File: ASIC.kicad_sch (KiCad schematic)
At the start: 76 parts, among them U1 MCP1824T-1202E/OT, U3 MCP1824T-1202E/OT, U4 MCP1824T-1202E/OT, U6 MCP1824T-1202E/OT, U8 SN74AXC4T774, Y2 50MHz

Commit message: move over to bitaxeBlock ASIC sheet
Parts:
- removed A1, A3: BZM2_MODE0, bitaxe:bzm2, symbol bitaxe:BZM2_mode0
- removed A2, A4: BZM2_MODE1, bitaxe:bzm2, symbol bitaxe:BZM2_mode1
- removed C19, C26, C27, C28, C7: 1uF, Capacitor_SMD:C_0402_1005Metric, symbol Device:C_Small
- removed C58: 0.1uF, Capacitor_SMD:C_0402_1005Metric, symbol Device:C_Small
- removed C60, C62, C63, C64: 120pF, Capacitor_SMD:C_0402_1005Metric, symbol Device:C_Small
- removed R4: 1k, Resistor_SMD:R_0402_1005Metric, symbol Device:R_Small_US
- removed R9: 10k, Resistor_SMD:R_0402_1005Metric, symbol Device:R_Small_US
- removed TP13, TP32, TP51, TP55: RSTI, bitaxe:TestPoint_Pad_1.0x0.4mm, symbol Connector:TestPoint
- removed TP14, TP31, TP38, TP46: RXO, bitaxe:TestPoint_Pad_1.0x0.4mm, symbol Connector:TestPoint
- removed TP17, TP33, TP40, TP50, TP54: TXO, bitaxe:TestPoint_Pad_1.0x0.4mm, symbol Connector:TestPoint
- removed TP18: 1V2-1, bitaxe:TestPoint_Pad_D1.0mm, symbol Connector:TestPoint
- removed TP20, TP36, TP52, TP56: RXI, bitaxe:TestPoint_Pad_1.0x0.4mm, symbol Connector:TestPoint
- removed TP21, TP34, TP41, TP49, TP53: TTO, bitaxe:TestPoint_Pad_1.0x0.4mm, symbol Connector:TestPoint
- removed TP22: GND, bitaxe:TestPoint_Pad_1.0x0.4mm, symbol Connector:TestPoint
- removed TP28, TP43: TTI, bitaxe:TestPoint_Pad_1.0x0.4mm, symbol Connector:TestPoint
- removed TP29, TP44: TXI, bitaxe:TestPoint_Pad_1.0x0.4mm, symbol Connector:TestPoint
- removed TP3: 1V2-3, bitaxe:TestPoint_Pad_D1.0mm, symbol Connector:TestPoint
- removed TP30, TP39, TP45: RSTO, bitaxe:TestPoint_Pad_1.0x0.4mm, symbol Connector:TestPoint
- removed TP35, TP48, TP57: CLKI, bitaxe:TestPoint_Pad_1.0x0.4mm, symbol Connector:TestPoint
- removed TP37, TP42, TP47: CLKO, bitaxe:TestPoint_Pad_1.0x0.4mm, symbol Connector:TestPoint
- removed TP58: D1, bitaxe:TestPoint_Pad_D1.0mm, symbol Connector:TestPoint
- removed TP59: D2, bitaxe:TestPoint_Pad_D1.0mm, symbol Connector:TestPoint
- removed TP60: D3, bitaxe:TestPoint_Pad_D1.0mm, symbol Connector:TestPoint
- removed U1, U3, U4, U6: MCP1824T-1202E/OT, bitaxe:SOT-23-5, symbol bitaxe:MCP1824
- removed U8: SN74AXC4T774, bitaxe:BQB0016A-MFG, symbol bitaxe:SN74AVC4T774-BQB
- removed Y2: 50MHz, bitaxe:OSC_ECS-3225MV-500-CN-TR, symbol bitaxe:oscillator
- added A1, A2: ProtoMC3, bitaxe:proto-mc3, symbol bitaxe:BlockMC3_mode0
- added A3, A4: ProtoMC3, bitaxe:proto-mc3, symbol bitaxe:BlockMC3_mode1
- added C100, C101, C102, C103, C104, C105, C106, C107, C108, C109, C110, C111, C112, C113, C114, C115, C116, C117, C118, C119, C120, C121, C122, C123, C124, C125, C126, C127, C128, C129, C209, C49, C50, C53, C54, C55, C56, C98, C99: 1uF, Capacitor_SMD:C_0402_1005Metric, symbol Device:C_Small
- added C130, C208, C51, C52, C84, C86, C88, C90, C91, C96: 0.1uF, Capacitor_SMD:C_0402_1005Metric, symbol Device:C_Small
- added C131, C79, C85, C87, C89, C92, C94, C97: 4.7uF, Capacitor_SMD:C_0402_1005Metric, symbol Device:C_Small
- added C66, C67, C69, C70, C71, C73, C74, C75, C78, C80, C81, C82, C83, C93, C95: 10uF, Capacitor_SMD:C_0603_1608Metric, symbol Device:C_Small
- added FB10, FB3, FB4, FB5, FB6, FB7, FB8, FB9: FerriteBead_Small, Inductor_SMD:L_0402_1005Metric, symbol Device:FerriteBead_Small
- added R25: 10k, Resistor_SMD:R_0402_1005Metric, symbol Device:R_Small_US
- added R70: 220k, Resistor_SMD:R_0402_1005Metric, symbol Device:R_US
- added R71: 1k, Resistor_SMD:R_0402_1005Metric, symbol Device:R_US
- added U13: TS3011, bitaxe:SOT-23-5, symbol bitaxe:TS3011
- added U14: SN74AVC2T45DCUR, bitaxeBlock:VSSOP-8_L2.1-W2.4-P0.50-LS3.2-BR, symbol bitaxeBlock:SN74AVC2T45DCUR
- added U15, U8: 25MHz, bitaxe:SMD3225-4P, symbol bitaxe:oscillator
- added U16, U18: TLV75512PDQNR, bitaxe:DQN0004A, symbol bitaxe:TLV755P
- added U17, U3: TLV755075PDQNR, bitaxe:DQN0004A, symbol bitaxe:TLV755P
- C25: LCSC C52923 -> (none)
- C57: value 0.1uF -> 1uF; DK 478-KGM05AR71C104KHCT-ND -> 587-5514-1-ND; LCSC C307331 -> (none); PARTNO KGM05AR71C104KH -> EMK105BJ105MV-F
- C59: LCSC C307331 -> (none)
- C61: value 120pF -> 0.1uF; DK 490-16458-1-ND -> 478-KGM05AR71C104KHCT-ND; PARTNO GCM1555C1H121FA16D -> KGM05AR71C104KH
- C68: value 1uF -> 10uF; footprint Capacitor_SMD:C_0402_1005Metric -> Capacitor_SMD:C_0603_1608Metric; DK 587-5514-1-ND -> 490-18214-1-ND; LCSC C52923 -> (none); PARTNO EMK105BJ105MV-F -> GRM188R61E106KA73D
- C72: value 1uF -> 0.1uF; DK 587-5514-1-ND -> (none); LCSC C52923 -> (none); PARTNO EMK105BJ105MV-F -> (none)
- R26: value 20k -> 12k; DK 311-20.0KLRCT-ND -> (none); PARTNO RC0402FR-0720KL -> (none)
- TP10: footprint bitaxe:TestPoint_Pad_D1.0mm -> TestPoint:TestPoint_Pad_D1.0mm
- TP11: value TTI -> CLKI; footprint bitaxe:TestPoint_Pad_1.0x0.4mm -> TestPoint:TestPoint_Pad_D1.0mm
- TP12: value TXI -> 1V2; footprint bitaxe:TestPoint_Pad_1.0x0.4mm -> TestPoint:TestPoint_Pad_D1.0mm
- TP2: value 1V2-2 -> 0V75-0; footprint bitaxe:TestPoint_Pad_D1.0mm -> TestPoint:TestPoint_Pad_D1.0mm
- TP4: value 1V2-4 -> 1V2-0; footprint bitaxe:TestPoint_Pad_D1.0mm -> TestPoint:TestPoint_Pad_D1.0mm
- TP6: value RSTI -> 0V75; footprint bitaxe:TestPoint_Pad_1.0x0.4mm -> TestPoint:TestPoint_Pad_D1.0mm
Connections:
- net 3V3: now also C61.1, C208.2, C209.2, R25.2, U13.5 (V+), U14.1 (VCCA); no longer C59.1
- net GND: now also C57.1, A1.10 (SEL0), A1.17 (VSS), A1.23 (VSS), A1.27 (VSS), A1.8 (SEL1), A1.9 (VSS), A2.10 (SEL0), A2.17 (VSS), A2.23 (VSS), A2.27 (VSS), A2.8 (SEL1), A2.9 (VSS), C101.2, C105.2, C114.2, C121.2, C208.1, C209.1, C51.1, C52.1, C53.1, C54.1, C56.1, C73.2, C74.2, C75.2, C78.2, C79.1, C80.2, C81.2, C82.2, C83.2, C84.1, C85.1, C86.1, C87.1, C91.1, C94.1, U13.2 (V-), U15.2 (GND), U17.2 (GND), U17.5 (PAD), U18.2 (GND), U18.5 (PAD), U8.2 (GND); no longer C57.2, C59.2, C68.1
- net RST_1V2: now also A1.19 (nRST), U14.6 (B2); no longer TP6.1
- net RST_3V3: now also U14.3 (A2)
- net RX_1V2: now also A1.24 (URXP), U14.7 (B1)
- net RX_3V3: now also U14.2 (A1)
- net TX_3V3: now also R70.2, U13.1
- net VDD: now also C68.1, A3.28 (VDD), A4.28 (VDD), C109.1, C110.1, C125.1, C126.1, C66.1, C67.1, C69.1, C70.1, C71.1, C93.1, C95.1
- net at R26.2: now also R25.1, U13.4 (-)
- net 1V2: now reaches TP12.1
- net 1V2: now also C57.2, C59.1, A2.21 (VDDIO12), C51.2, C52.2, C86.2, C87.2, C91.2, C94.2, FB4.2, FB6.2, U14.5 (DIR), U14.8 (VCCB), U15.4 (VIN), U18.1 (VOUT), U8.1 (EN), U8.4 (VIN)
- net CLKI-0: now reaches TP11.1
- net CLKI-0: now also A3.1 (CLKI), U15.3 (OUT)
- net 1V2-1 renamed 0V75
- net 0V75: now also TP6.1, A2.22 (VDDH), C56.2, C79.2, C84.2, C85.2, FB3.2, FB5.2, U17.1 (VOUT); no longer C57.1
- net 1V2-2 renamed 0V75-0
- net 0V75-0: now also A3.22 (VDDH), C50.2, C88.2, C89.2, C96.2, C97.2, FB7.2, FB9.2, U3.1 (VOUT)
- net 1V2-4 renamed 1V2-0
- net 1V2-0: now also A3.21 (VDDIO12), A3.8 (SEL1), A4.8 (SEL1), C130.2, C131.2, C55.2, C90.2, C92.2, FB10.2, FB8.2, U15.1 (EN), U16.1 (VOUT)
- net 5V_SWITCH renamed 5V
- net 5V: now also C49.2, C53.2, C54.2, U16.3 (EN), U16.4 (VIN), U17.3 (EN), U17.4 (VIN), U18.3 (EN), U18.4 (VIN), U3.3 (EN), U3.4 (VIN); no longer C68.2
- net GND3 renamed GND0
- net GND0: now also C68.2, A1.28 (VDD), A2.28 (VDD), A3.10 (SEL0), A3.17 (VSS), A3.23 (VSS), A3.27 (VSS), A3.9 (VSS), A4.10 (SEL0), A4.17 (VSS), A4.23 (VSS), A4.27 (VSS), A4.9 (VSS), C102.1, C106.2, C113.2, C117.1, C118.1, C122.2, C129.2, C130.1, C131.1, C49.1, C50.1, C55.1, C66.2, C67.2, C69.2, C70.2, C71.2, C73.1, C74.1, C75.1, C78.1, C80.1, C81.1, C82.1, C83.1, C88.1, C89.1, C90.1, C92.1, C93.2, C95.2, C96.1, C97.1, C98.1, U16.2 (GND), U16.5 (PAD), U3.2 (GND), U3.5 (PAD)
- net GND4: no longer names the net of C61.2
- net GND4: now also C59.2, U14.4 (GND)
- net REFCLKIN1 renamed CLKI
- net CLKI: now also A1.26 (CLKI), U8.3 (OUT)
- new net: A4.12 (VDDI2_0), C127.2, C128.1
- new net: A4.11 (VDDI1_0), C128.2, C129.1
- new net: A4.15 (VDDI2_1), C123.1, C124.2
- new net: A4.16 (VDDI1_1), C122.1, C123.2
- new net: R70.1, R71.2, U13.3 (+)
- new net: A2.12 (VDDI2_0), C100.1, C99.2
- new net: A2.11 (VDDI1_0), C100.2, C101.1
- new net: A3.26 (CLKO), A4.1 (CLKI)
- new net: A4.13 (VDDI3_0), C126.2, C127.1
- new net: A4.14 (VDDI3_1), C124.1, C125.2
- new net: A3.24 (UTXP), A4.3 (URXP)
- new net: A4.5 (VDDH), FB9.1
- new net: A4.6 (VDDIO12), FB10.1
- new net: A2.15 (VDDI2_1), C103.2, C104.1
- new net: A2.16 (VDDI1_1), C104.2, C105.1
- new net: A1.11 (VDDI1_0), C120.2, C121.1
- new net: A3.11 (VDDI1_0), C112.2, C113.1
- new net: A3.12 (VDDI2_0), C111.2, C112.1
- new net: A3.13 (VDDI3_0), C110.2, C111.1
- new net: A3.14 (VDDI3_1), C108.1, C109.2
- new net: A3.15 (VDDI2_1), C107.1, C108.2
- new net: A3.16 (VDDI1_1), C106.1, C107.2
- new net: A3.5 (VDDH), FB7.1
- new net: A3.6 (VDDIO12), FB8.1
- new net: A2.14 (VDDI3_1), C102.2, C103.1
- new net: A1.14 (VDDI3_1), C116.1, C117.2
- new net: A1.15 (VDDI2_1), C115.1, C116.2
- new net: A1.6 (VDDIO12), FB6.1
- new net: A2.6 (VDDIO12), FB4.1
- new net: A2.13 (VDDI3_0), C98.2, C99.1
- new net: A1.3 (UTXP), A2.24 (URXP)
- new net: A1.1 (CLKO), A2.26 (CLKI)
- new net: A2.5 (VDDH), FB3.1
- new net: A1.12 (VDDI2_0), C119.2, C120.1
- new net: A1.13 (VDDI3_0), C118.2, C119.1
- new net: A1.16 (VDDI1_1), C114.1, C115.2
- new net: A1.5 (VDDH), FB5.1
- new net Level Shifter/RST_IN: A2.7 (nRST)
- new net Level Shifter/RST_OUT: A3.7 (nRST)
- new net Level Shifter/TX_IN: A2.3 (UTXP)
- new net Level Shifter/TX_OUT: A3.3 (URXP)
- new net TX_2V4: A4.24 (UTXP), R71.1
- new net nRST_1V2: A2.19 (nRST)
- no-connect marks 30 -> 18
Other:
- removed sheet bypass1-1
- removed sheet bypass1-2
- removed sheet bypass2-1
- removed sheet bypass2-2
- removed sheet bypass3-1
- removed sheet bypass3-2
- removed sheet bypass4-1
- removed sheet bypass4-2
- removed sheet shifter1-2
- removed sheet shifter2-3
- removed sheet shifter3-4
- added sheet Level Shifter (level_shifter.kicad_sch)
- note added: "0.75V LDO"
- note added: "1.2V LDO"
- note removed: "->"
- note removed: "<-"
- note removed: "DOMAIN 1"
- note removed: "DOMAIN 2"
- note removed: "DOMAIN 3"
- note removed: "DOMAIN 4"

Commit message: add footprints and some 3d cad. rough part placements
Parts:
- TP10, TP11, TP12, TP2, TP4, TP6: footprint TestPoint:TestPoint_Pad_D1.0mm -> bitaxe:TestPoint_Pad_D1.0mm
- U14: footprint bitaxeBlock:VSSOP-8_L2.1-W2.4-P0.50-LS3.2-BR -> bitaxe:VSSOP-8_L2.1-W2.4-P0.50-LS3.2-BR; symbol bitaxeBlock:SN74AVC2T45DCUR -> bitaxe:SN74AVC2T45DCUR
- U16, U18: DK 296-51785-1-ND -> 296-TLV755075PDQNRCT-ND; PARTNO TLV75512PDQNR -> TLV755075PDQNR
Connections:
- net nRST_1V2 is gone; now on an unnamed net: A2.19 (nRST)
- net at A4.7 (nRST): now also A3.19 (nRST)
- net 5V renamed 5V_SWITCH
- no-connect marks 18 -> 23

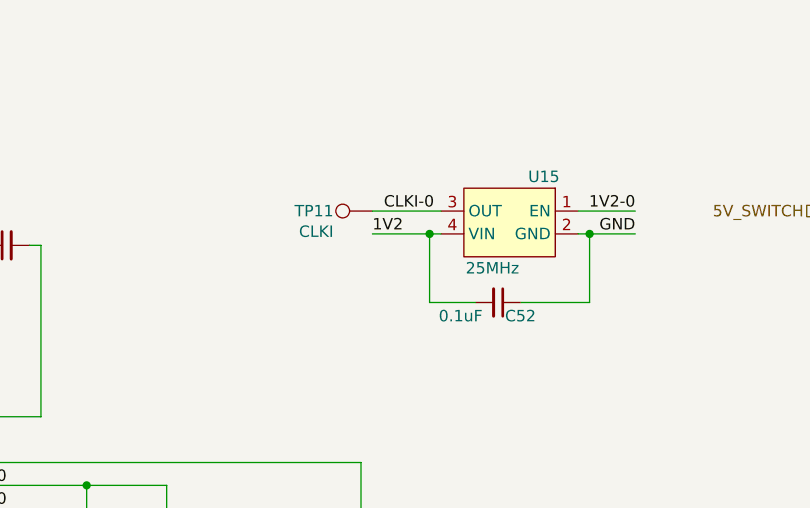
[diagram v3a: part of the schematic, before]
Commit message: a lot more rough component placement
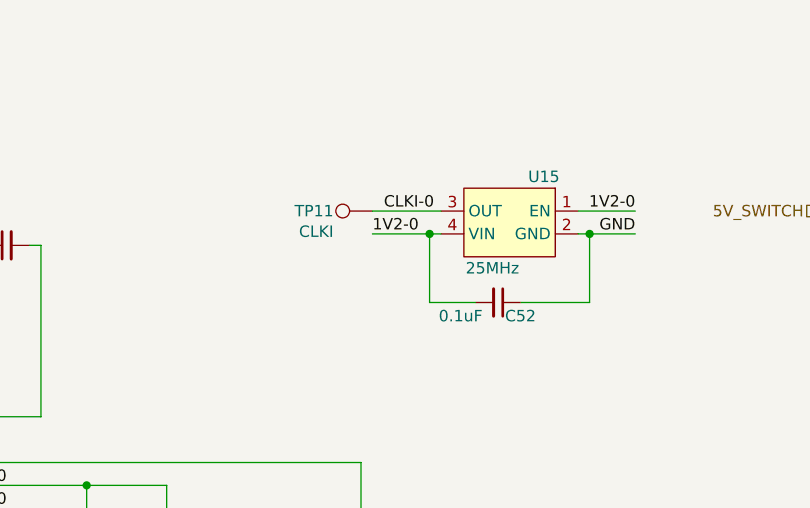
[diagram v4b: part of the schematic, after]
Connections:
- net 1V2: no longer C52.2, U15.4 (VIN)
- net 1V2-0: now also C52.2, U15.4 (VIN)
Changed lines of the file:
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@@
 		)
 	)
-	(label "1V2"
+	(label "1V2-0"
 		(at 433.07 104.14 0)
 		(effects

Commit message: routing progress
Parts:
- removed FB10, FB3, FB4, FB5, FB6, FB7, FB8, FB9: FerriteBead_Small, Inductor_SMD:L_0402_1005Metric, symbol Device:FerriteBead_Small
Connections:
- net 0V75: now also A1.5 (VDDH), A2.5 (VDDH)
- net 0V75-0: now also A3.5 (VDDH), A4.5 (VDDH)
- net 1V2: now also A1.6 (VDDIO12), A2.6 (VDDIO12)
- net 1V2-0: now also A3.6 (VDDIO12), A4.6 (VDDIO12)
- net GND: no longer C52.1, U15.2 (GND)
- net GND0: now also C52.1, U15.2 (GND)
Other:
- moved on the sheet: C51, C59, C61, TP10, U14, U8

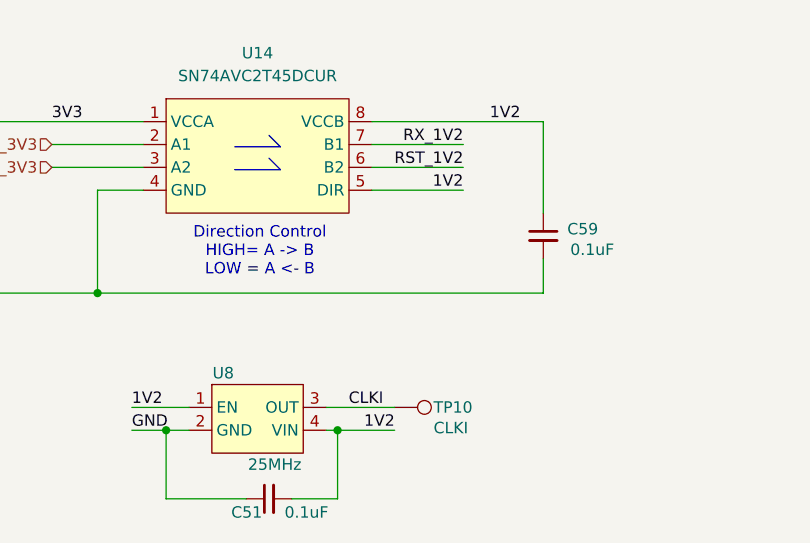
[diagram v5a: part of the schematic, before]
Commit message: remove old bzm2 stuff
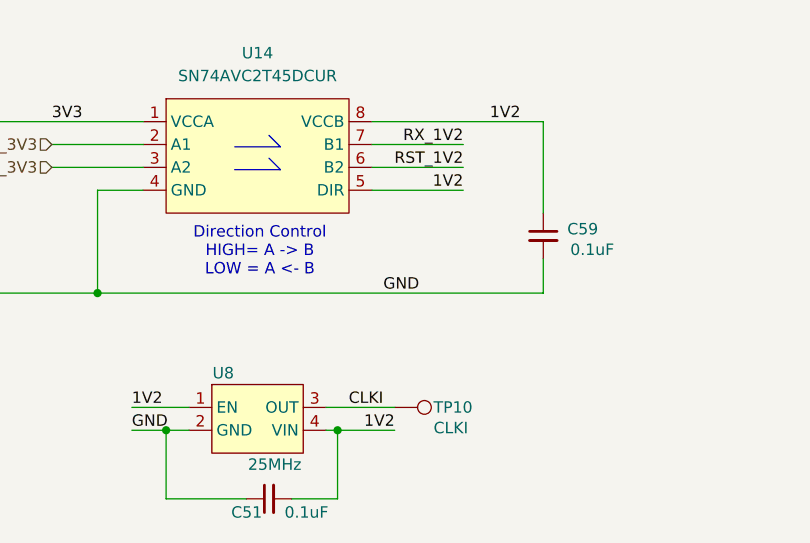
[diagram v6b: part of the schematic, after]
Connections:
- net GND: now also C59.2, C61.2, U14.4 (GND)
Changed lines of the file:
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@@
+		)
+	)
+	(label "GND"
+		(at 128.27 233.68 0)
+		(effects
+			(font
+				(size 1.27 1.27)
+			)
+			(justify left bottom)
 		)
 	)

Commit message: add more data test points. Fix ERC & DRC issues
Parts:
- added TP14: RST, bitaxe:TestPoint_Pad_D1.0mm, symbol Connector:TestPoint
- added TP15: RX, bitaxe:TestPoint_Pad_D1.0mm, symbol Connector:TestPoint
- added TP16: GND, bitaxe:TestPoint_Pad_D1.0mm, symbol Connector:TestPoint
- added TP41, TP44, TP51, TP56, TP57: RST, bitaxe:TestPoint_Pad_1.0x0.4mm, symbol Connector:TestPoint
- added TP42, TP49: TX, bitaxe:TestPoint_Pad_1.0x0.4mm, symbol Connector:TestPoint
- added TP43, TP45, TP47, TP50: RX, bitaxe:TestPoint_Pad_1.0x0.4mm, symbol Connector:TestPoint
- added TP46, TP48: CLK, bitaxe:TestPoint_Pad_1.0x0.4mm, symbol Connector:TestPoint
- added TP52, TP53, TP54, TP55, TP58, TP59: GND, bitaxe:TestPoint_Pad_1.0x0.4mm, symbol Connector:TestPoint
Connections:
- net GND: now also TP16.1, TP53.1, TP54.1, TP58.1, TP59.1
- net GND0: now also TP52.1, TP55.1
- net Level Shifter/RST_IN: now also TP41.1
- net Level Shifter/RST_OUT: now also TP44.1
- net Level Shifter/TX_IN: now also TP42.1
- net Level Shifter/TX_OUT: now also TP43.1
- net RST_1V2: now also TP51.1
- net RST_3V3: now also TP14.1
- net RX_1V2: now also TP50.1
- net RX_3V3: now also TP15.1
- net TX_2V4: now also TP49.1
- net at A3.26 (CLKO), A4.1 (CLKI): now also TP46.1
- net at A3.24 (UTXP), A4.3 (URXP): now also TP45.1
- net at A3.19 (nRST), A4.7 (nRST): now also TP56.1
- net at A1.7 (nRST), A2.19 (nRST): now also TP57.1
- net at A1.3 (UTXP), A2.24 (URXP): now also TP47.1
- net at A1.1 (CLKO), A2.26 (CLKI): now also TP48.1
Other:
- moved on the sheet: C59

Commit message: update schematic BOM and some part substitutions
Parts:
- C100, C101, C102, C103, C104, C105, C106, C107, C108, C109, C110, C111, C112, C113, C114, C115, C116, C117, C118, C119, C120, C121, C122, C123, C124, C125, C126, C127, C128, C129, C209, C25, C49, C50, C53, C54, C55, C56, C57, C98, C99: LCSC (none) -> C52923
- C130, C72, C84, C86, C88, C90, C91, C96: DK (none) -> 490-10700-1-ND; LCSC (none) -> C77020; PARTNO (none) -> GRM155R71H104KE14D; Voltage (none) -> 50V
- C131, C79, C85, C87, C89, C92, C94, C97: DK (none) -> 490-14306-1-ND; PARTNO (none) -> GRM155R61A475MEAAD
- C208, C59, C61: DK 478-KGM05AR71C104KHCT-ND -> 490-10700-1-ND; LCSC (none) -> C77020; PARTNO KGM05AR71C104KH -> GRM155R71H104KE14D; Voltage (none) -> 50V
- C51, C52: DK 1276-1234-1-ND -> 490-10700-1-ND; LCSC (none) -> C77020; PARTNO CL05A104KO5NNNC -> GRM155R71H104KE14D; Voltage (none) -> 50V
- C66, C67, C68, C69, C70, C71, C73, C74, C75, C78, C80, C81, C82, C83, C93, C95: Voltage (none) -> 25V
- R25: DK (none) -> 311-10KJRCT-ND; LCSC (none) -> C25744; PARTNO (none) -> RC0402JR-0710KL
- R26: DK (none) -> 311-12.0KLRCT-ND; PARTNO (none) -> RC0402FR-0712KL
- R70: DK (none) -> 311-220KLRCT-ND; PARTNO (none) -> RC0402FR-07220KL
- U14: DK (none) -> 296-17993-1-ND; LCSC (none) -> C140318; LCSC Part C140318 -> (none); PARTNO (none) -> SN74AVC2T45DCUR
